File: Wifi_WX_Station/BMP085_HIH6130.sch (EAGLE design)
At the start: 8 parts, among them U1 HIH_6130

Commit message: updated BOM with all prices- As Checked in to BATCH PCB
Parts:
- removed JP1: (no value), Headers:PINHD-1X6
- added JP2: (no value), wifi_WX:M05PTH
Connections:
- net +3V3: now also JP2.5; no longer JP1.6
- net GND: now also JP2.1; no longer JP1.1
- net SCL: now also JP2.4; no longer JP1.4
- net SDA: now also JP2.3; no longer JP1.3
- net XCLR: now also JP2.2; no longer JP1.2
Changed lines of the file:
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@@
 <setting verticaltext="up"/>
 </settings>
-<grid distance="0.1" unitdist="inch" unit="inch" style="lines" multiple="1" display="no" altdistance="0.01" altunitdist="inch" altunit="inch"/>
+<grid distance="0.05" unitdist="inch" unit="inch" style="lines" multiple="1" display="no" altdistance="0.025" altunitdist="inch" altunit="inch"/>
 <layers>
 <layer number="1" name="Top" color="4" fill="1" visible="no" active="no"/>
@@
 <layer number="53" name="tPadExt" color="7" fill="1" visible="no" active="no"/>
 <layer number="54" name="bPadExt" color="1" fill="1" visible="no" active="no"/>
+<layer number="56" name="wert" color="7" fill="1" visible="no" active="no"/>
 <layer number="91" name="Nets" color="2" fill="1" visible="yes" active="yes"/>
 <layer number="92" name="Busses" color="1" fill="1" visible="yes" active="yes"/>
@@
 <layer number="100" name="Moduls" color="14" fill="0" visible="yes" active="yes"/>
 <layer number="101" name="Flex-Kleb" color="1" fill="7" visible="no" active="yes"/>
+<layer number="102" name="Vscore" color="7" fill="1" visible="yes" active="yes"/>
+<layer number="103" name="tMap" color="7" fill="1" visible="yes" active="yes"/>
+<layer number="104" name="Name" color="16" fill="1" visible="yes" active="yes"/>
 <layer number="105" name="Beschreib" color="9" fill="1" visible="no" active="yes"/>
 <layer number="106" name="BGA-Top" color="4" fill="1" visible="no" active="yes"/>
 <layer number="107" name="BD-Top" color="5" fill="1" visible="no" active="yes"/>
+<layer number="116" name="Patch_BOT" color="9" fill="4" visible="yes" active="yes"/>
 <layer number="121" name="_tsilk" color="7" fill="1" visible="yes" active="yes"/>
 <layer number="122" name="_bsilk" color="7" fill="1" visible="yes" active="yes"/>
+<layer number="125" name="_tNames" color="7" fill="1" visible="yes" active="yes"/>
+<layer number="144" name="Drill_legend" color="7" fill="1" visible="yes" active="yes"/>
+<layer number="151" name="HeatSink" color="7" fill="1" visible="yes" active="yes"/>
+<layer number="199" name="Contour" color="7" fill="1" visible="yes" active="yes"/>
 <layer number="200" name="200bmp" color="1" fill="10" visible="no" active="no"/>
 <layer number="201" name="201bmp" color="2" fill="1" visible="no" active="no"/>
 <layer number="202" name="202bmp" color="3" fill="1" visible="no" active="no"/>
+<layer number="203" name="203bmp" color="4" fill="10" visible="yes" active="yes"/>
+<layer number="204" name="204bmp" color="5" fill="10" visible="yes" active="yes"/>
+<layer number="205" name="205bmp" color="6" fill="10" visible="yes" active="yes"/>
+<layer number="206" name="206bmp" color="7" fill="10" visible="yes" active="yes"/>
+<layer number="207" name="207bmp" color="8" fill="10" visible="yes" active="yes"/>
+<layer number="208" name="208bmp" color="9" fill="10" visible="yes" active="yes"/>
+<layer number="209" name="209bmp" color="7" fill="1" visible="yes" active="yes"/>
+<layer number="210" name="210bmp" color="7" fill="1" visible="yes" active="yes"/>
+<layer number="211" name="211bmp" color="7" fill="1" visible="yes" active="yes"/>
+<layer number="212" name="212bmp" color="7" fill="1" visible="yes" active="yes"/>
+<layer number="213" name="213bmp" color="7" fill="1" visible="yes" active="yes"/>
+<layer number="214" name="214bmp" color="7" fill="1" visible="yes" active="yes"/>
+<layer number="215" name="215bmp" color="7" fill="1" visible="yes" active="yes"/>
+<layer number="216" name="216bmp" color="7" fill="1" visible="yes" active="yes"/>
+<layer number="217" name="217bmp" color="18" fill="1" visible="no" active="no"/>
+<layer number="218" name="218bmp" color="19" fill="1" visible="no" active="no"/>
+<layer number="219" name="219bmp" color="20" fill="1" visible="no" active="no"/>
+<layer number="220" name="220bmp" color="21" fill="1" visible="no" active="no"/>
+<layer number="221" name="221bmp" color="22" fill="1" visible="no" active="no"/>
+<layer number="222" name="222bmp" color="23" fill="1" visible="no" active="no"/>
+<layer number="223" name="223bmp" color="24" fill="1" visible="no" active="no"/>
+<layer number="224" name="224bmp" color="25" fill="1" visible="no" active="no"/>
 <layer number="250" name="Descript" color="3" fill="1" visible="no" active="no"/>
 <layer number="251" name="SMDround" color="12" fill="11" visible="no" active="no"/>
+<layer number="254" name="cooling" color="7" fill="1" visible="yes" active="yes"/>
 </layers>
 <schematic>
@@
 <part name="+3V1" library="supply1" deviceset="+3V3" device=""/>
 <part name="C3" library="rcl" deviceset="CPOL-US" device="SMCB" value="22uF/10V"/>
-<part name="JP1" library="Headers" deviceset="PINHD-1X6" device=""/>
 <part name="U1" library="Stofer" deviceset="HIH_6130" device=""/>
 <part name="C4" library="rcl" deviceset="C-US" device="C0805K" value="100nF"/>
 <part name="U2" library="1AA_Stofer" deviceset="BMP085" device=""/>
+<part name="JP2" library="wifi_WX" deviceset="M05" device="PTH"/>
 </parts>
 <sheets>
@@
 <instance part="+3V1" gate="G$1" x="66.04" y="81.28"/>
 <instance part="C3" gate="G$1" x="12.7" y="10.16"/>
-<instance part="JP1" gate="A" x="-2.54" y="53.34" rot="R180"/>
 <instance part="U1" gate="G$1" x="45.72" y="7.62"/>
 <instance part="C4" gate="G$1" x="35.56" y="22.86"/>
 <instance part="U2" gate="G$1" x="121.92" y="48.26"/>
+<instance part="JP2" gate="G$1" x="-3.81" y="50.8"/>
 </instances>
 <busses>
@@
 <wire x1="83.82" y1="50.8" x2="83.82" y2="25.4" width="0.1524" layer="91"/>
 <wire x1="83.82" y1="50.8" x2="83.82" y2="58.42" width="0.1524" layer="91"/>
-<wire x1="83.82" y1="50.8" x2="0" y2="50.8" width="0.1524" layer="91"/>
+<wire x1="83.82" y1="50.8" x2="3.81" y2="50.8" width="0.1524" layer="91"/>
 <junction x="83.82" y="50.8"/>
-<label x="-12.7" y="49.53" size="1.778" layer="95"/>
+<label x="8.636" y="51.308" size="1.778" layer="95"/>
 <pinref part="R2" gate="G$1" pin="1"/>
-<pinref part="JP1" gate="A" pin="3"/>
 <pinref part="U1" gate="G$1" pin="SDA"/>
 <wire x1="73.66" y1="25.4" x2="83.82" y2="25.4" width="0.1524" layer="91"/>
@@
 <pinref part="U2" gate="G$1" pin="SDA"/>
 <wire x1="93.98" y1="55.88" x2="109.22" y2="55.88" width="0.1524" layer="91"/>
+<pinref part="JP2" gate="G$1" pin="3"/>
 </segment>
 </net>
@@
 <wire x1="78.74" y1="53.34" x2="78.74" y2="33.02" width="0.1524" layer="91"/>
 <wire x1="78.74" y1="53.34" x2="78.74" y2="58.42" width="0.1524" layer="91"/>
-<wire x1="78.74" y1="53.34" x2="0" y2="53.34" width="0.1524" layer="91"/>
+<wire x1="78.74" y1="53.34" x2="3.81" y2="53.34" width="0.1524" layer="91"/>
 <junction x="78.74" y="53.34"/>
-<label x="-12.7" y="52.07" size="1.778" layer="95"/>
+<label x="8.89" y="53.975" size="1.778" layer="95"/>
 <pinref part="R1" gate="G$1" pin="1"/>
-<pinref part="JP1" gate="A" pin="4"/>
 <pinref part="U1" gate="G$1" pin="SCL"/>
 <wire x1="73.66" y1="33.02" x2="78.74" y2="33.02" width="0.1524" layer="91"/>
@@
 <pinref part="U2" gate="G$1" pin="SCK"/>
 <wire x1="101.6" y1="50.8" x2="109.22" y2="50.8" width="0.1524" layer="91"/>
+<pinref part="JP2" gate="G$1" pin="4"/>
 </segment>
 </net>
@@
 <wire x1="27.94" y1="0" x2="35.56" y2="0" width="0.1524" layer="91"/>
 <wire x1="35.56" y1="0" x2="99.06" y2="0" width="0.1524" layer="91"/>
-<wire x1="0" y1="45.72" x2="7.62" y2="45.72" width="0.1524" layer="91"/>
+<wire x1="3.81" y1="45.72" x2="7.62" y2="45.72" width="0.1524" layer="91"/>
 <wire x1="7.62" y1="45.72" x2="7.62" y2="0" width="0.1524" layer="91"/>
-<label x="-12.7" y="44.45" size="1.778" layer="95"/>
+<label x="8.255" y="44.45" size="1.778" layer="95"/>
 <pinref part="GND1" gate="1" pin="GND"/>
-<pinref part="JP1" gate="A" pin="1"/>
 <pinref part="U1" gate="G$1" pin="VSS"/>
 <wire x1="40.64" y1="17.78" x2="35.56" y2="17.78" width="0.1524" layer="91"/>
@@
 <pinref part="C2" gate="G$1" pin="2"/>
 <wire x1="27.94" y1="5.08" x2="27.94" y2="0" width="0.1524" layer="91"/>
+<pinref part="JP2" gate="G$1" pin="1"/>
 </segment>
 </net>
@@
 <wire x1="66.04" y1="76.2" x2="20.32" y2="76.2" width="0.1524" layer="91"/>
 <wire x1="20.32" y1="76.2" x2="7.62" y2="76.2" width="0.1524" layer="91"/>
-<wire x1="7.62" y1="58.42" x2="7.62" y2="76.2" width="0.1524" layer="91"/>
-<wire x1="0" y1="58.42" x2="7.62" y2="58.42" width="0.1524" layer="91"/>
-<label x="-12.7" y="57.15" size="1.778" layer="95"/>
+<wire x1="7.62" y1="55.88" x2="7.62" y2="76.2" width="0.1524" layer="91"/>
+<wire x1="3.81" y1="55.88" x2="7.62" y2="55.88" width="0.1524" layer="91"/>
+<label x="8.255" y="57.785" size="1.778" layer="95"/>
 <pinref part="R2" gate="G$1" pin="2"/>
 <pinref part="R1" gate="G$1" pin="2"/>
 <pinref part="+3V1" gate="G$1" pin="+3V3"/>
-<pinref part="JP1" gate="A" pin="6"/>
 <pinref part="U1" gate="G$1" pin="VDD"/>
 <wire x1="40.64" y1="33.02" x2="20.32" y2="33.02" width="0.1524" layer="91"/>
@@
 <wire x1="12.7" y1="25.4" x2="12.7" y2="12.7" width="0.1524" layer="91"/>
 <wire x1="20.32" y1="33.02" x2="20.32" y2="25.4" width="0.1524" layer="91"/>
+<pinref part="JP2" gate="G$1" pin="5"/>
 </segment>
 </net>
 <net name="XCLR" class="0">
 <segment>
-<wire x1="93.98" y1="48.26" x2="0" y2="48.26" width="0.1524" layer="91"/>
-<label x="-12.7" y="46.99" size="1.778" layer="95"/>
-<pinref part="JP1" gate="A" pin="2"/>
+<wire x1="93.98" y1="48.26" x2="3.81" y2="48.26" width="0.1524" layer="91"/>
+<label x="8.255" y="48.26" size="1.778" layer="95"/>
 <wire x1="93.98" y1="48.26" x2="93.98" y2="45.72" width="0.1524" layer="91"/>
 <pinref part="U2" gate="G$1" pin="XCLR"/>
 <wire x1="93.98" y1="45.72" x2="109.22" y2="45.72" width="0.1524" layer="91"/>
-</segment>
-</net>
+<pinref part="JP2" gate="G$1" pin="2"/>
+</segment>
+</net>

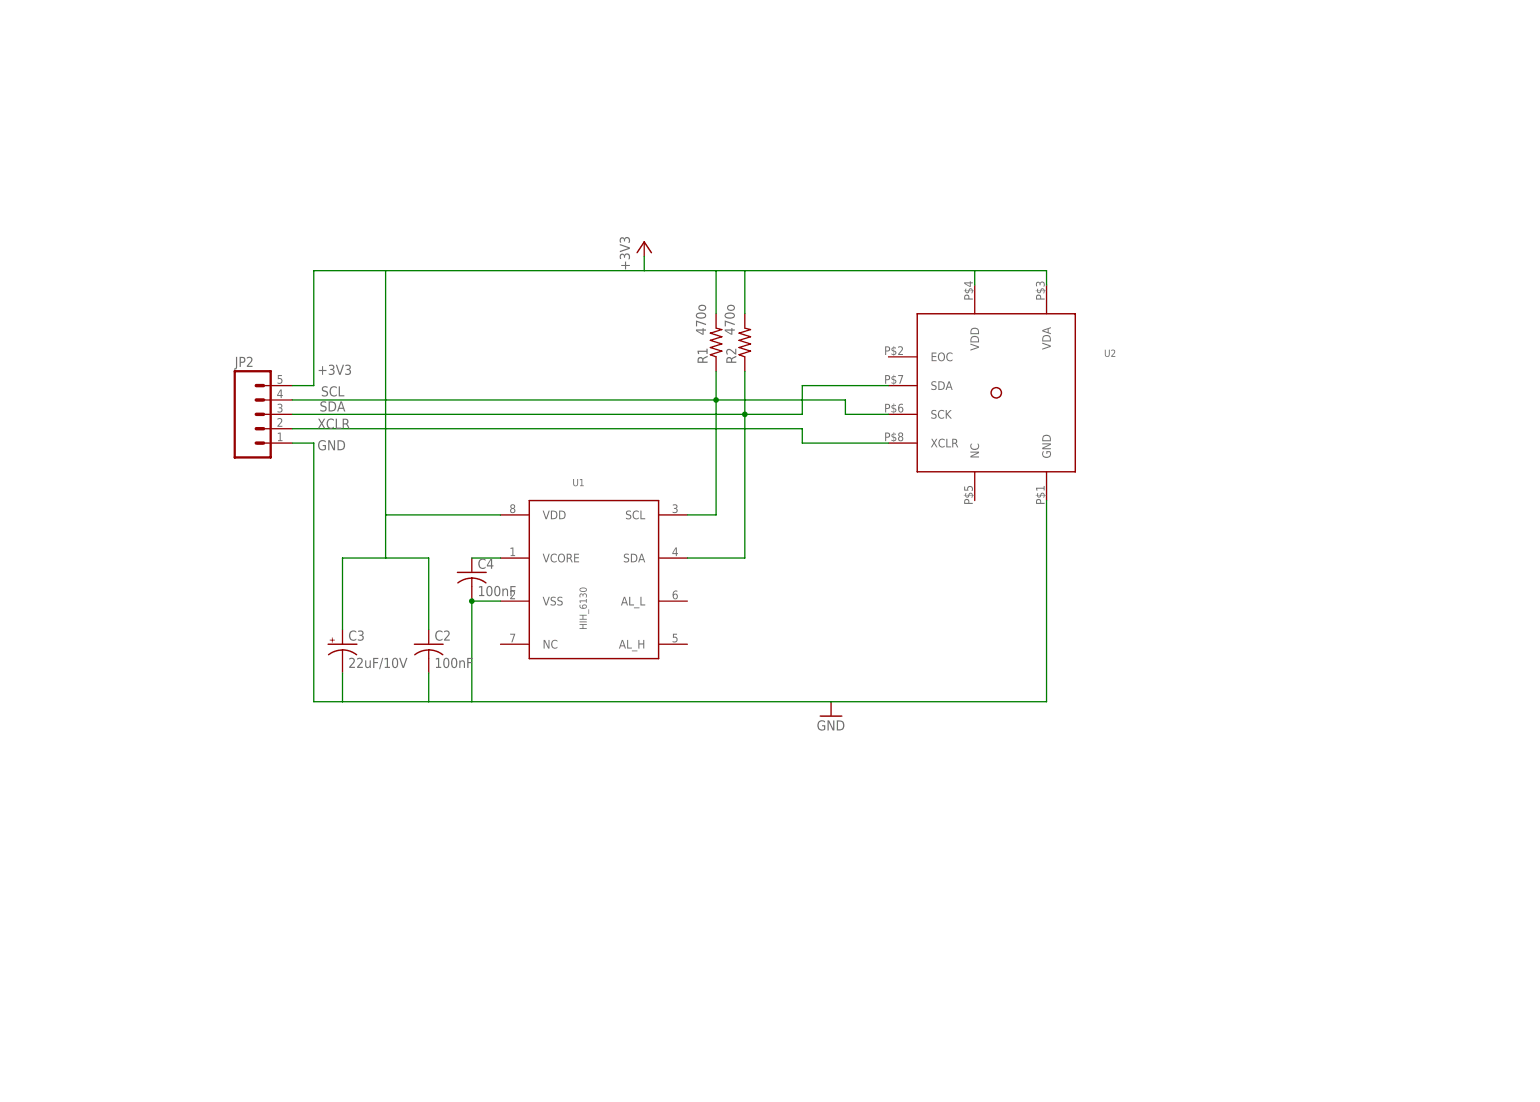
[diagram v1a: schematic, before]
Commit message: Added multiple new boards - H-pwrdist- Insp_Wind_enc, 5040 etc..
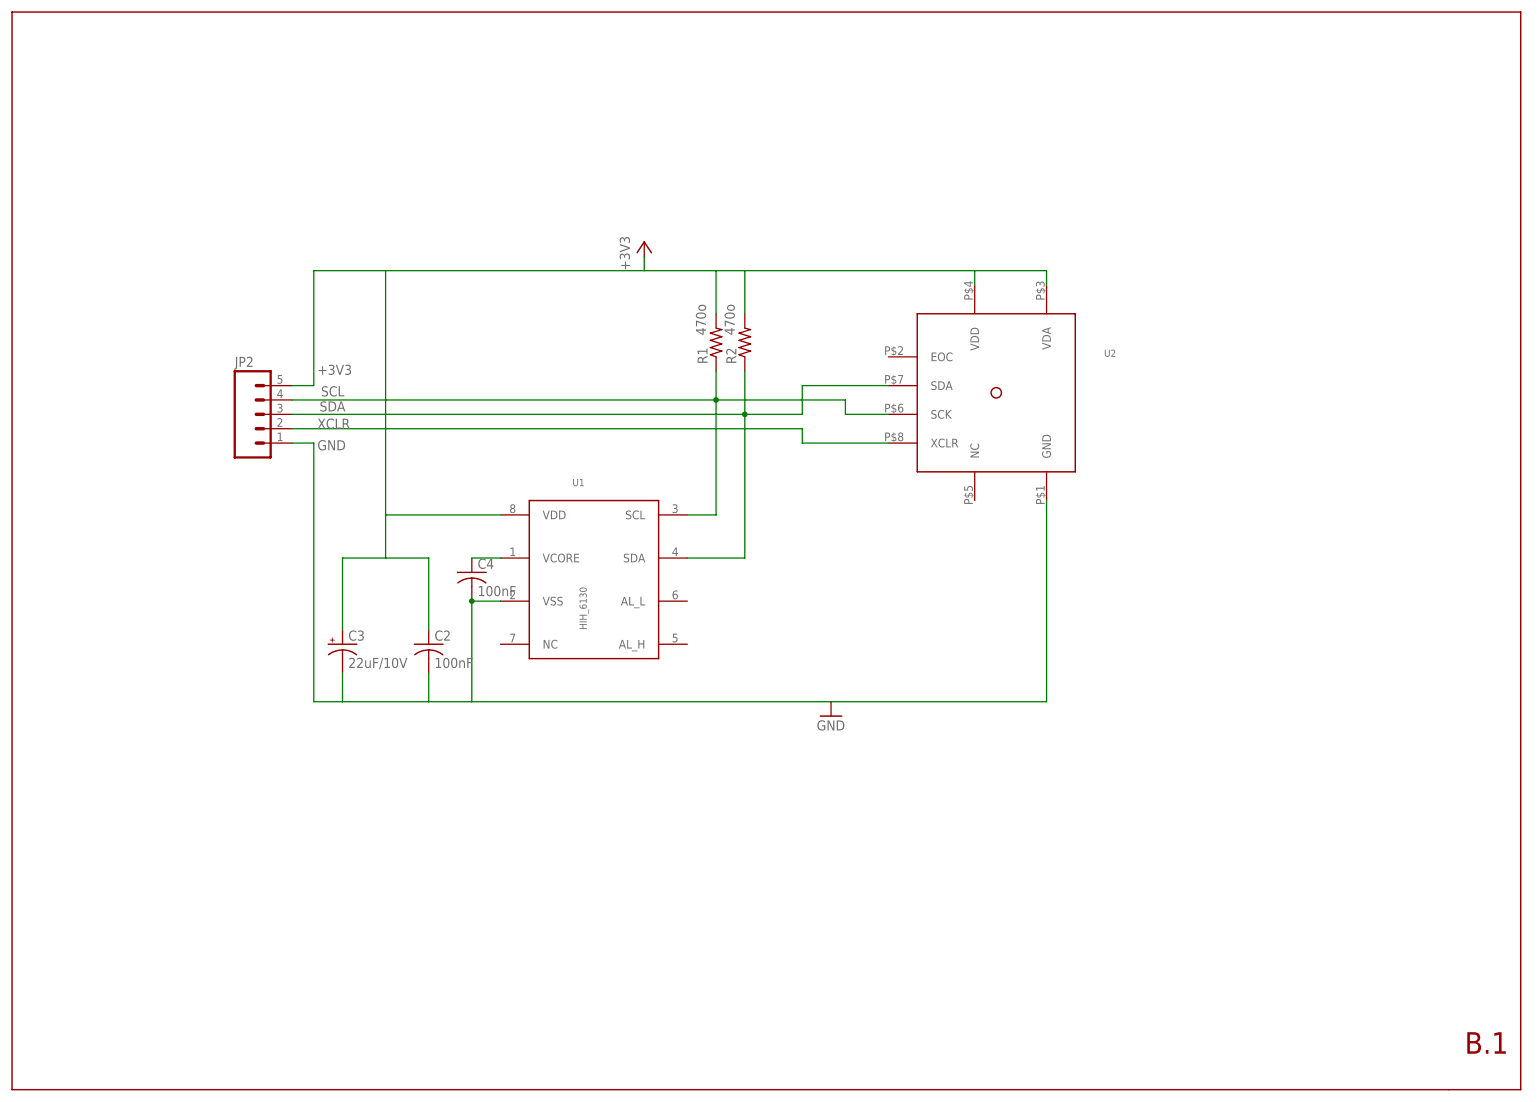
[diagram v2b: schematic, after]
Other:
- note added: "B.1"
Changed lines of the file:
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@@
 <setting verticaltext="up"/>
 </settings>
-<grid distance="0.05" unitdist="inch" unit="inch" style="lines" multiple="1" display="no" altdistance="0.025" altunitdist="inch" altunit="inch"/>
+<grid distance="0.1" unitdist="inch" unit="inch" style="lines" multiple="1" display="no" altdistance="0.01" altunitdist="inch" altunit="inch"/>
 <layers>
 <layer number="1" name="Top" color="4" fill="1" visible="no" active="no"/>
@@
 <part name="U2" library="1AA_Stofer" deviceset="BMP085" device=""/>
 <part name="JP2" library="wifi_WX" deviceset="M05" device="PTH"/>
+<part name="U$1" library="1AA_Stofer" deviceset="8.5X11" device=""/>
 </parts>
 <sheets>
 <sheet>
 <plain>
+<text x="211.074" y="-62.23" size="3.81" layer="94">B.1</text>
 </plain>
 <instances>
@@
 <instance part="U2" gate="G$1" x="121.92" y="48.26"/>
 <instance part="JP2" gate="G$1" x="-3.81" y="50.8"/>
+<instance part="U$1" gate="G$1" x="-45.72" y="-68.58"/>
+<instance part="U$1" gate="G$2" x="119.38" y="-68.58"/>
 </instances>
 <busses>
